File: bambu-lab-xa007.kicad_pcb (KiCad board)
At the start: 2 copper layers, 32 x 20 mm, 7 parts, among them J1 Side_B, J2 Side_A, SW1 SW_SPDT

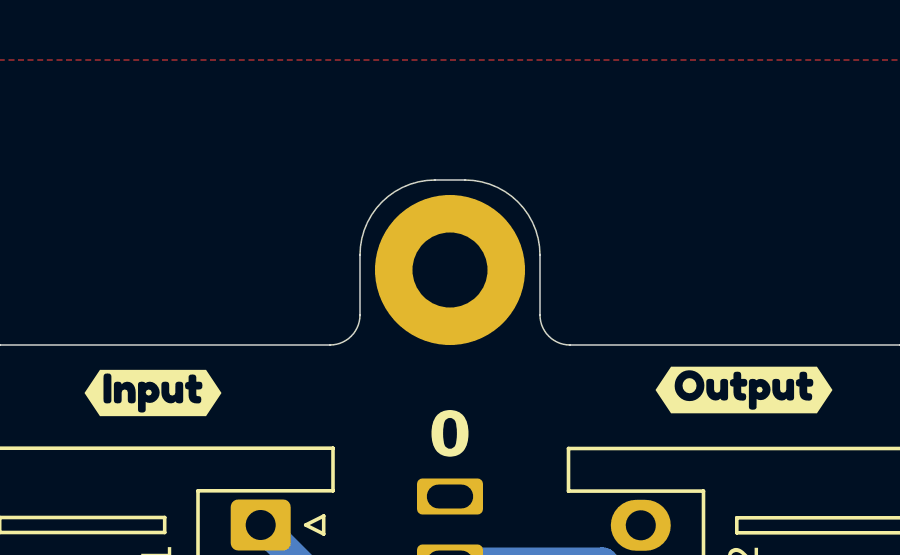
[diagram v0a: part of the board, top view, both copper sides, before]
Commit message: fix: modify footprint for mounting hole to be M2.5
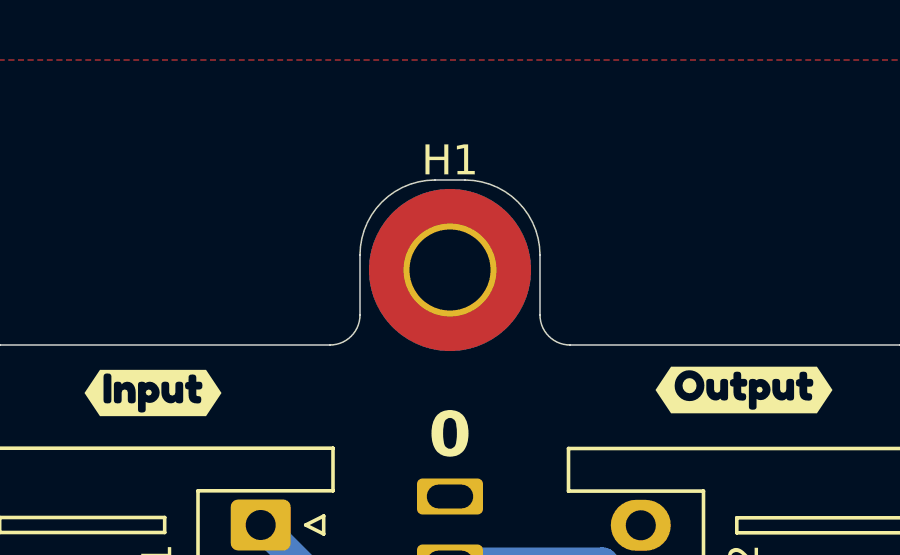
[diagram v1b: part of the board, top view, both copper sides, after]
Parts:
- removed REF**: OSHW-Symbol_6.7x6mm_SilkScreen, Symbol:OSHW-Symbol_6.7x6mm_SilkScreen
- H1: footprint MountingHole:MountingHole_2.5mm_Pad -> MountingHole:MountingHole_2.7mm_M2.5_Pad_TopBottom
